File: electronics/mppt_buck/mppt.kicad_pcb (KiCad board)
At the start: 2 copper layers, 62.5 x 65.5 mm, 49 parts, among them J1 I2C, J2 UART, J3 In, J4 In, J5 Out, J6 Out, Q1 IRLR2705TRPBF, Q2 IRLR2705TRPBF, SW1 SW_DIP_x01, U1 AD8211, U2 AD8211, U3 ATmega328P-A, U4 2EDN852x, U5 L78L15_SO8, Y1 16.00M-SMDHC49S

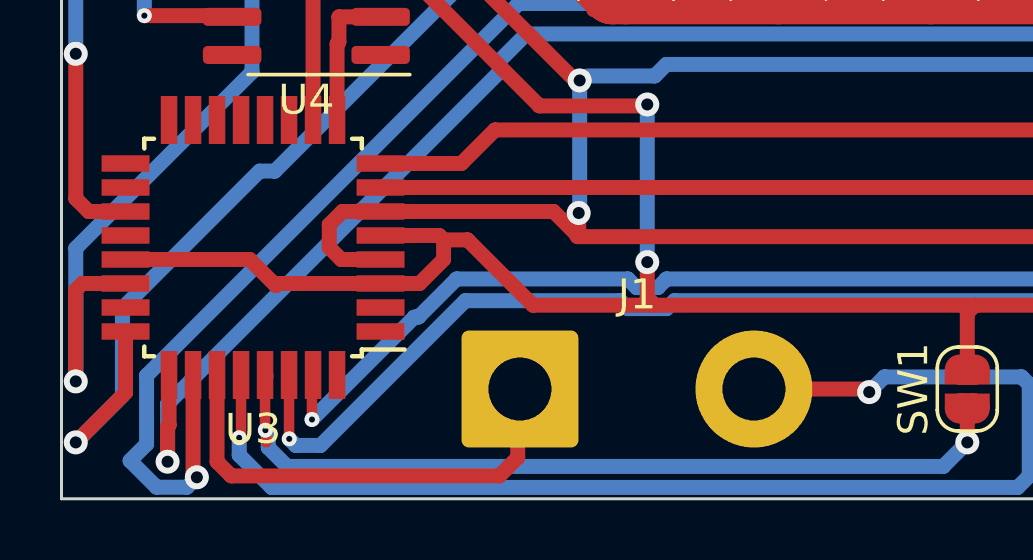
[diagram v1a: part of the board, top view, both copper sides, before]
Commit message: mppt cpu reset fix
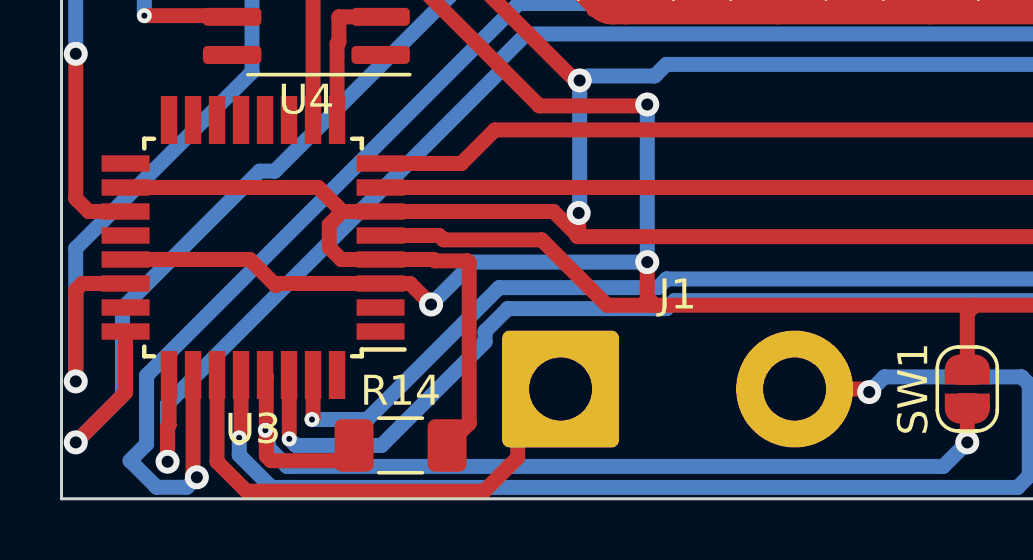
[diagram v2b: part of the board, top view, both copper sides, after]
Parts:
- added R14: 10k, Resistor_SMD:R_1206_3216Metric_Pad1.30x1.75mm_HandSolder, F.Cu at (101.7, 107.7)
- moved J1 1.36 mm to (107.1, 105.8)
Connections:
- U3 pad 18: unconnected-(U3-Pad18) -> +5V
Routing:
- net +5V: track 153.9 -> 170.9 mm
- net GND: track 390.0 -> 396.7 mm, vias 4 -> 5
- net Net-(R14-Pad1): track 28.0 -> 33.8 mm

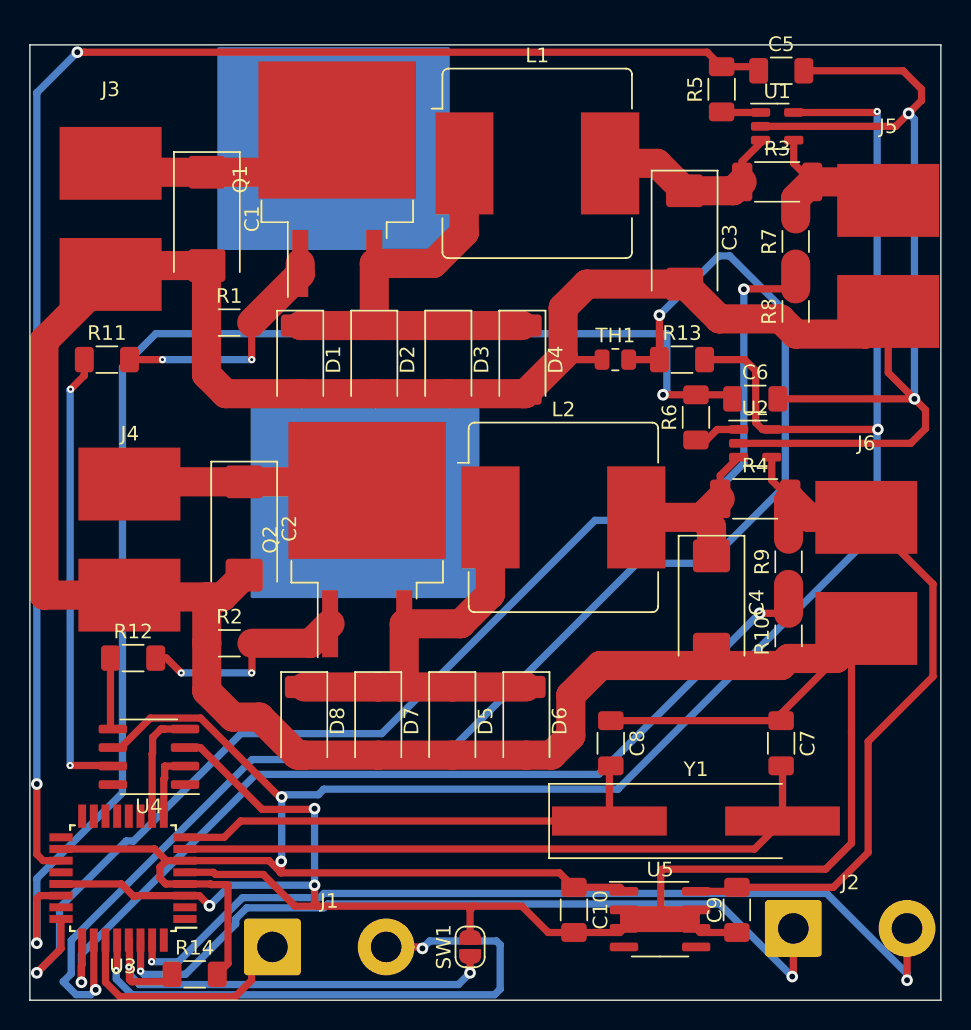
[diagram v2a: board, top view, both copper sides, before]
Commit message: mppt part list corrected
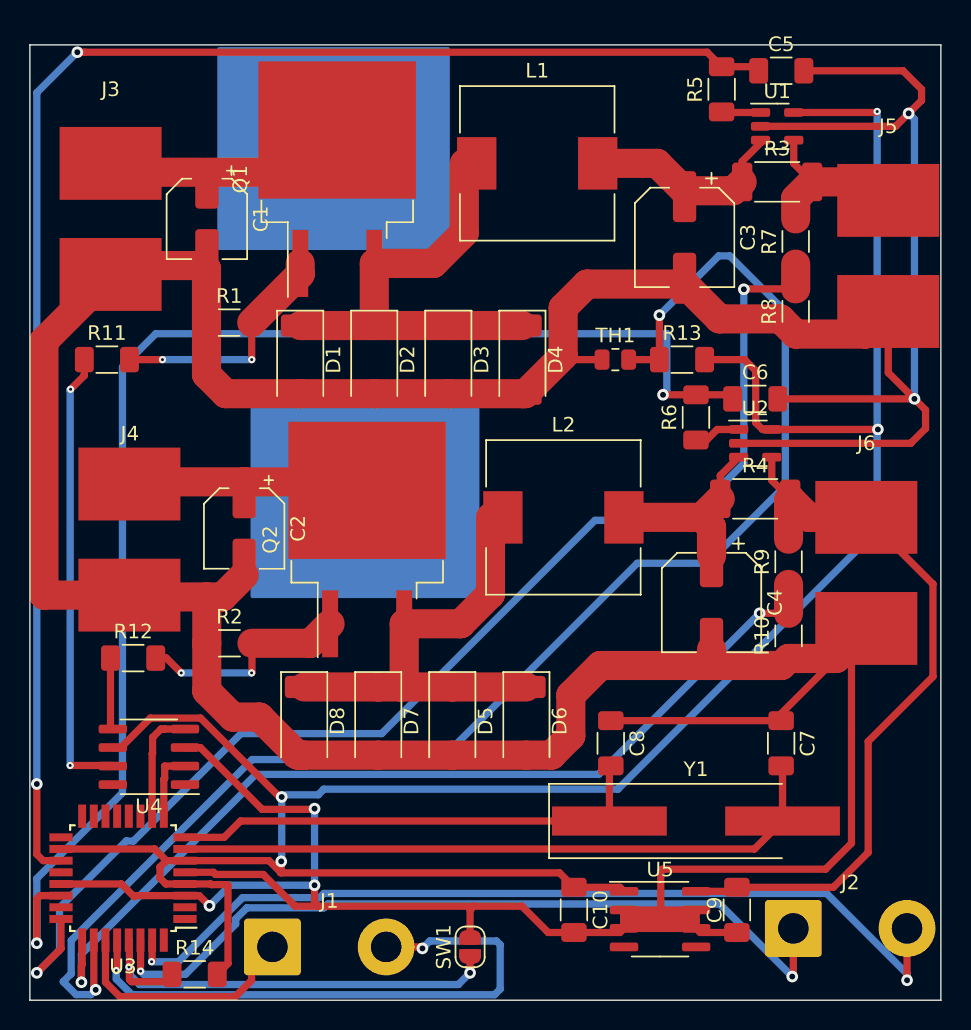
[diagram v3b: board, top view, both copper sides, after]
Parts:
- C1, C2: footprint Capacitor_Tantalum_SMD:CP_EIA-7343-15_Kemet-W_Pad2.25x2.55mm_HandSolder -> Capacitor_SMD:CP_Elec_5x5.4
- C3, C4: footprint Capacitor_Tantalum_SMD:CP_EIA-7343-15_Kemet-W_Pad2.25x2.55mm_HandSolder -> Capacitor_SMD:CP_Elec_6.3x5.4
- L1, L2: footprint Inductor_SMD:L_Bourns_SRR1208_12.7x12.7mm -> Inductor_SMD:L_10.4x10.4_H4.8
- U1, U2: value AD8211 -> INA180A4IDBVT
- U4: value 2EDN852x -> IX4427N
- U5: value L78L15_SO8 -> DI78L05DAB
